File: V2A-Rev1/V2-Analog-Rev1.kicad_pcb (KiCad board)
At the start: 2 copper layers, 116.3 x 70 mm, 45 parts, among them J1 Apple II, J2 DB15_Female_HighDensity_Mount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, J3 NOPAL/GAL, J4 NONWIFI, J5 VGA, J6 VGA, U1 SN74LVC8T245DGVR, U2 SN74LVC8T245DGVR, U3 SN74LVC8T245DGVR, U4 SN74LVC8T245DGVR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

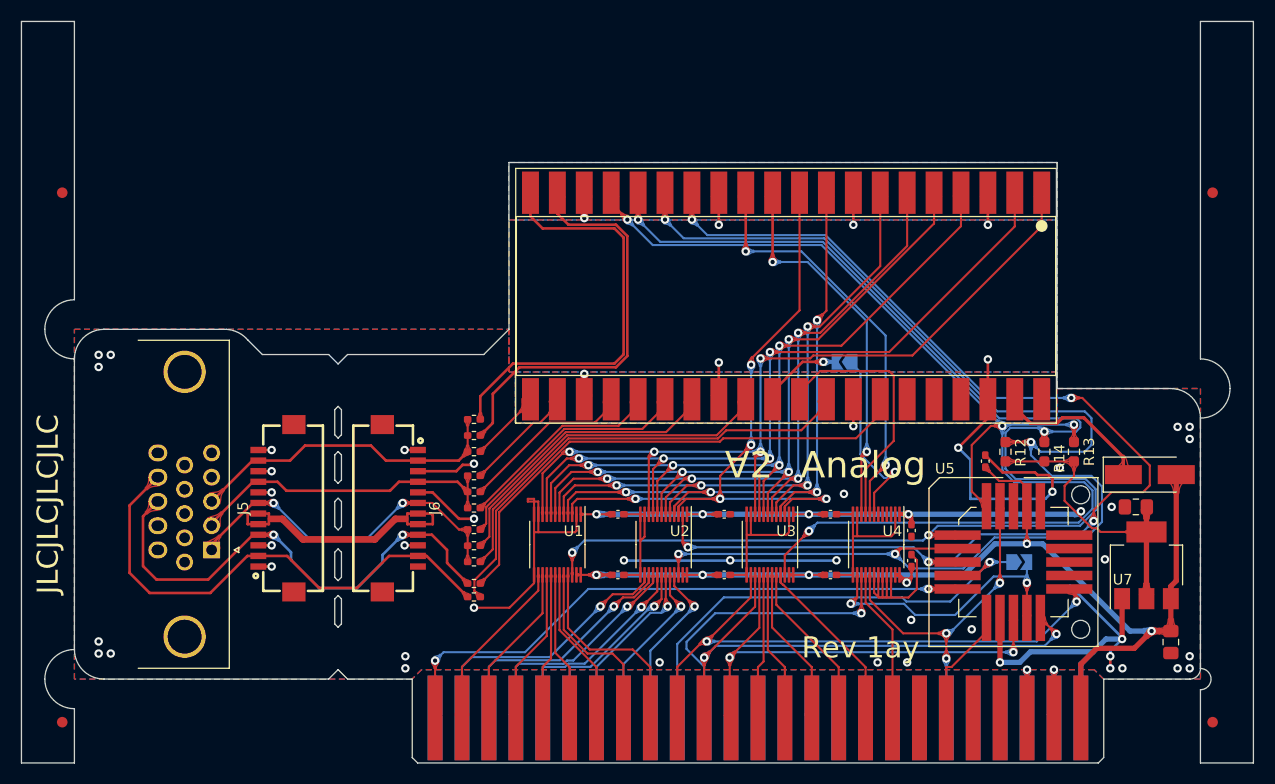
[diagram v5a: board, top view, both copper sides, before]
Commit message: Added V-scoring suggestion to VGA break-away port. Added to Silkscreen MicroUSB port location from PICO.
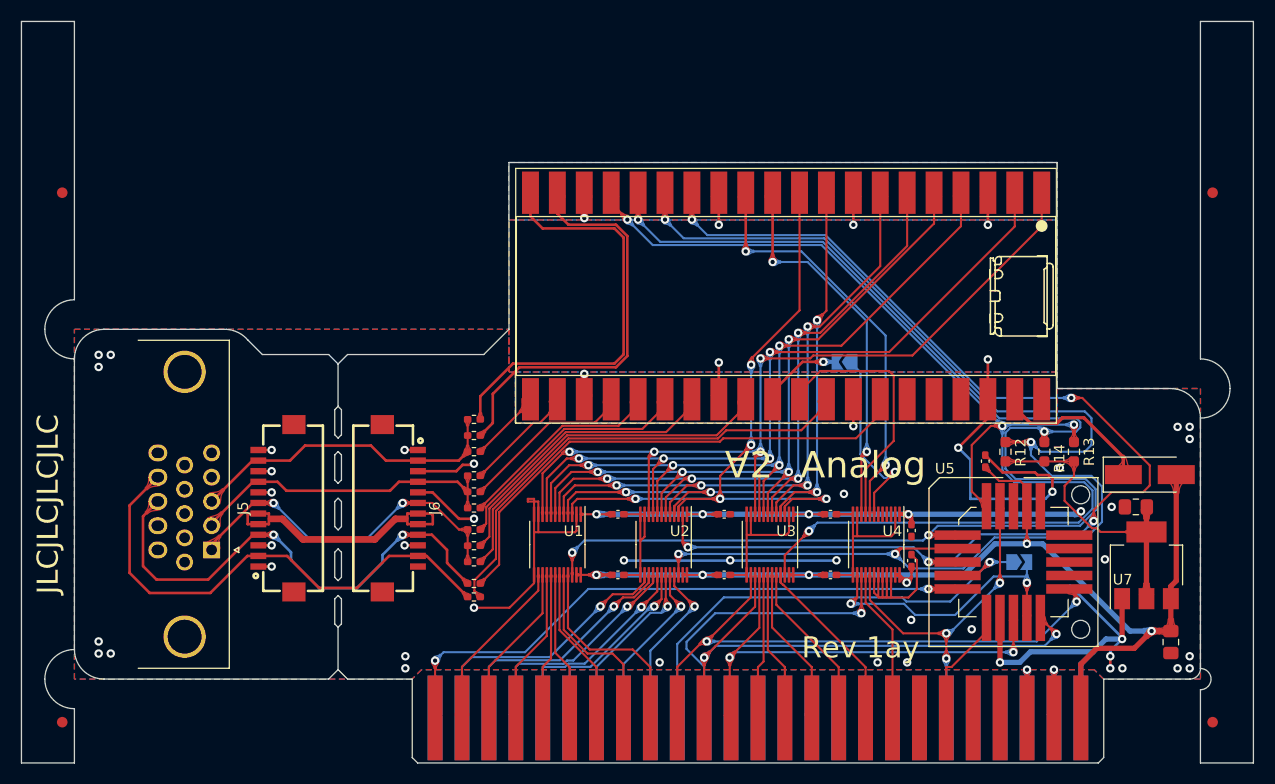
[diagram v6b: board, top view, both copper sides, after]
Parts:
- added ?: , clipboard:e3534cc3-c0d5-4838-9122-8c22cc37e6f7, F.Cu at (169.4, 84.1)
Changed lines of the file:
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@@
     )
+  )
+  (footprint "clipboard:e3534cc3-c0d5-4838-9122-8c22cc37e6f7" (layer "F.Cu")
+    (at 169.401495 84.06 -90)
+    (attr board_only exclude_from_pos_files exclude_from_bom)
+    (fp_text reference "" (at 0 0 90) (layer "F.SilkS")
+      (effects (font (size 1.27 1.27) (thickness 0.15)))
+    )
+    (fp_text value "" (at 0 0 90) (layer "F.SilkS")
+      (effects (font (size 1.27 1.27) (thickness 0.15)))
+    )
+    (fp_line (start 9.95 5.349995) (end 2.775 5.349995) (layer "F.SilkS") (width 0.15))
+    (fp_line (start 8.8 4.824995) (end 8.8 4.624995) (layer "F.SilkS") (width 0.15))
+    (fp_line (start 4.675 5.399995) (end 3.875 5.399995) (layer "F.SilkS") (width 0.15))
+    (fp_line (start 10.175 -0.000005) (end 2.575 -0.000005) (layer "F.SilkS") (width 0.15))
+    (fp_line (start 2.775 5.074995) (end 3.025 5.074995) (layer "F.SilkS") (width 0.15))
+    (fp_line (start 9.8 4.924995) (end 9.8 5.049995) (layer "F.SilkS") (width 0.15))
+    (fp_line (start 6.85 4.624995) (end 6.85 5.349995) (layer "F.SilkS") (width 0.15))
+    (fp_line (start 9.45 -0.000005) (end 9.45 -0.225005) (layer "F.SilkS") (width 0.15))
+    (fp_line (start 9.1 -0.575005) (end 3.6 -0.575005) (layer "F.SilkS") (width 0.15))
+    (fp_line (start 3.2 4.324995) (end 2.65 4.324995) (layer "F.SilkS") (width 0.15))
+    (fp_line (start 3.6322 0) (end 3.8354 0.2794) (layer "F.SilkS") (width 0.15))
+    (fp_line (start 10.1 4.324995) (end 9.55 4.324995) (layer "F.SilkS") (width 0.15))
+    (fp_line (start 3.025 5.074995) (end 3.025 4.899995) (layer "F.SilkS") (width 0.15))
+    (fp_line (start 2.575 -0.000005) (end 2.575 0.899995) (layer "F.SilkS") (width 0.15))
+    (fp_line (start 4.7 4.899995) (end 4.7 4.599995) (layer "F.SilkS") (width 0.15))
+    (fp_line (start 10.125 4.424995) (end 10.125 -0.000005) (layer "F.SilkS") (width 0.15))
+    (fp_line (start 3.375 4.824995) (end 3.375 4.499995) (layer "F.SilkS") (width 0.15))
+    (fp_line (start 3.025 4.899995) (end 5.85 4.899995) (layer "F.SilkS") (width 0.15))
+    (fp_line (start 9.35 4.524995) (end 9.35 4.749995) (layer "F.SilkS") (width 0.15))
+    (fp_line (start 6.05 4.449995) (end 6.675 4.449995) (layer "F.SilkS") (width 0.15))
+    (fp_line (start 10.175 0.899995) (end 10.175 -0.000005) (layer "F.SilkS") (width 0.15))
+    (fp_line (start 8.025 4.549995) (end 8.025 4.899995) (layer "F.SilkS") (width 0.15))
+    (fp_line (start 8.875 5.399995) (end 8.075 5.399995) (layer "F.SilkS") (width 0.127))
+    (fp_line (start 3.8354 0.2794) (end 8.8646 0.2794) (layer "F.SilkS") (width 0.15))
+    (fp_line (start 2.625 -0.000005) (end 2.625 4.499995) (layer "F.SilkS") (width 0.15))
+    (fp_line (start 2.775 5.349995) (end 2.775 5.074995) (layer "F.SilkS") (width 0.15))
+    (fp_line (start 9.95 5.049995) (end 9.95 5.349995) (layer "F.SilkS") (width 0.15))
+    (fp_line (start 8.8646 0.2794) (end 9.0678 0) (layer "F.SilkS") (width 0.15))
+    (fp_line (start 6.85 4.899995) (end 9.65 4.899995) (layer "F.SilkS") (width 0.15))
+    (fp_line (start 3.275 -0.250005) (end 3.275 -0.000005) (layer "F.SilkS") (width 0.15))
+    (fp_line (start 9.8 5.049995) (end 9.95 5.049995) (layer "F.SilkS") (width 0.15))
+    (fp_line (start 3.9 4.599995) (end 3.9 4.899995) (layer "F.SilkS") (width 0.15))
+    (fp_line (start 5.85 5.349995) (end 5.85 4.649995) (layer "F.SilkS") (width 0.15))
+    (fp_arc (start 3.45 4.899995) (mid 3.396998 4.877998) (end 3.375 4.824995) (layer "F.SilkS") (width 0.15))
+    (fp_arc (start 3.2 4.324995) (mid 3.323745 4.376251) (end 3.375 4.499995) (layer "F.SilkS") (width 0.15))
+    (fp_arc (start 8.875 4.899995) (mid 8.821939 4.878057) (end 8.8 4.824995) (layer "F.SilkS") (width 0.15))
+    (fp_arc (start 6.675 4.449995) (mid 6.798745 4.501251) (end 6.85 4.624995) (layer "F.SilkS") (width 0.15))
+    (fp_arc (start 3.9 4.599995) (mid 4.017159 4.317156) (end 4.3 4.199995) (layer "F.SilkS") (width 0.15))
+    (fp_arc (start 4.3 4.199995) (mid 4.582844 4.317152) (end 4.7 4.599995) (layer "F.SilkS") (width 0.15))
+    (fp_arc (start 9.1 -0.575005) (mid 9.347489 -0.472493) (end 9.45 -0.225005) (layer "F.SilkS") (width 0.15))
+    (fp_arc (start 8.025 4.549995) (mid 8.127514 4.302511) (end 8.375 4.199995) (layer "F.SilkS") (width 0.15))
+    (fp_arc (start 10.125001 4.424994) (mid 9.985879 4.760874) (end 9.65 4.899995) (layer "F.SilkS") (width 0.15))
+    (fp_arc (start 9.35 4.749995) (mid 9.306068 4.856064) (end 9.2 4.899995) (layer "F.SilkS") (width 0.15))
+    (fp_arc (start 9.35 4.524995) (mid 9.40858 4.383577) (end 9.55 4.324995) (layer "F.SilkS") (width 0.15))
+    (fp_arc (start 8.375 4.199995) (mid 8.675522 4.324474) (end 8.8 4.624995) (layer "F.SilkS") (width 0.15))
+    (fp_arc (start 3.025001 4.899994) (mid 2.74216 4.782837) (end 2.625 4.499995) (layer "F.SilkS") (width 0.15))
+    (fp_arc (start 5.85 4.649995) (mid 5.90858 4.508577) (end 6.05 4.449995) (layer "F.SilkS") (width 0.15))
+    (fp_arc (start 3.275 -0.250005) (mid 3.370192 -0.479811) (end 3.6 -0.575005) (layer "F.SilkS") (width 0.15))
   )
   (footprint "Fiducial:Fiducial_1mm_Mask2mm" (layer "F.Cu")
@@
   (gr_line (start 93.948 94.556) (end 95.327 95.935) (layer "Edge.Cuts") (width 0.05))
   (gr_line (start 188.88 134.492) (end 188.88 64.492) (layer "Edge.Cuts") (width 0.05))
+  (gr_line (start 102.473 125.683) (end 102.473 121.683) (layer "Edge.Cuts") (width 0.05))
   (gr_poly
     (pts
@@
   (gr_line (start 183.88 134.492) (end 183.88 127.576) (layer "Edge.Cuts") (width 0.05))
   (gr_arc (start 186.674 99.144) (mid 185.855656 101.119656) (end 183.88 101.938) (layer "Edge.Cuts") (width 0.05))
+  (gr_line (start 102.473 100.828) (end 102.473 96.828) (layer "Edge.Cuts") (width 0.05))
   (gr_line (start 102.473 96.828) (end 101.58 95.935) (layer "Edge.Cuts") (width 0.05))
   (gr_arc (start 183.88 125.576) (mid 184.88 126.576) (end 183.88 127.576) (layer "Edge.Cuts") (width 0.05))
